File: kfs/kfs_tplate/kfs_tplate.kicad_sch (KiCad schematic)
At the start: 76 parts, among them SW0 SWITCH, SW1 SWITCH, SW10 SWITCH, SW11 SWITCH, SW12 SWITCH, SW13 SWITCH, SW14 SWITCH, SW15 SWITCH, SW16 SWITCH, SW17 SWITCH, SW18 SWITCH, SW19 SWITCH, SW2 SWITCH, SW20 SWITCH, SW21 SWITCH, SW22 SWITCH, SW23 SWITCH, SW24 SWITCH, SW25 SWITCH, SW26 SWITCH, SW27 SWITCH, SW28 SWITCH, SW29 SWITCH, SW3 SWITCH, SW30 SWITCH, SW31 SWITCH, SW32 SWITCH, SW33 SWITCH, SW34 SWITCH, SW35 SWITCH, SW36 SWITCH, SW37 SWITCH, SW38 SWITCH, SW39 SWITCH, SW4 SWITCH, SW40 SWITCH, SW41 SWITCH, SW42 SWITCH, SW43 SWITCH, SW44 SWITCH, SW45 SWITCH, SW46 SWITCH, SW47 SWITCH, SW48 SWITCH, SW49 SWITCH, SW5 SWITCH, SW50 SWITCH, SW51 SWITCH, SW52 SWITCH, SW53 SWITCH, SW54 SWITCH, SW55 SWITCH, SW56 SWITCH, SW57 SWITCH, SW58 SWITCH, SW59 SWITCH, SW6 SWITCH, SW60 SWITCH, SW61 SWITCH, SW62 SWITCH, SW63 SWITCH, SW7 SWITCH, SW8 SWITCH, SW9 SWITCH, U0 ARDUINO_PRO_MICRO

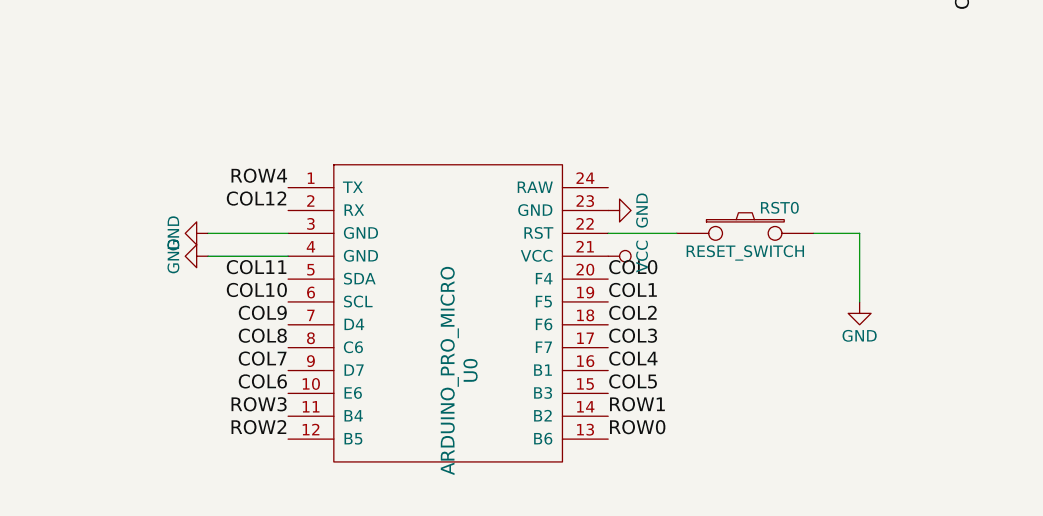
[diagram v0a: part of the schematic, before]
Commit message: Many updates to kfs. Now low profile.
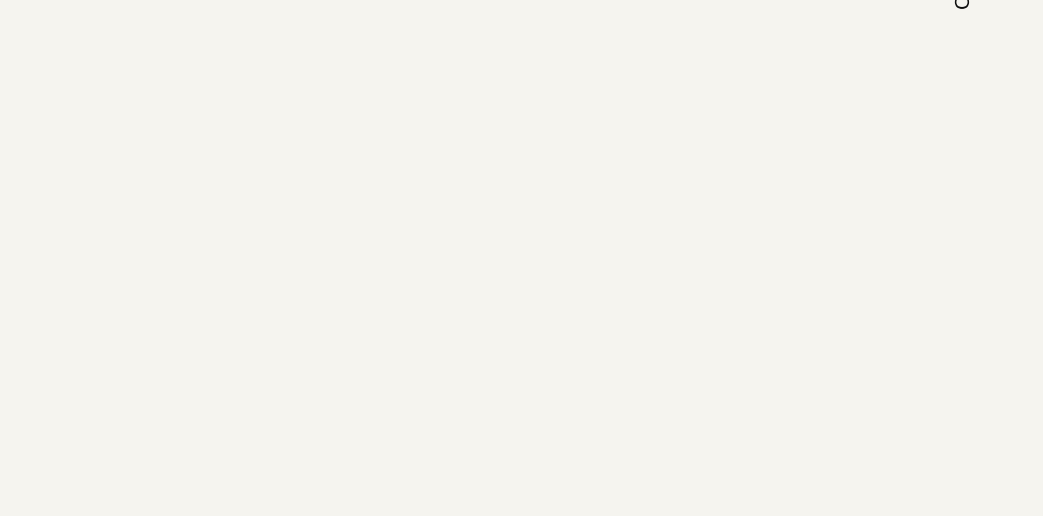
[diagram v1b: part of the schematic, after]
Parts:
- removed RST0: RESET_SWITCH, footprints:reset_button, symbol symbols:SWITCH_PUSH
- removed U0: ARDUINO_PRO_MICRO, ProMicro_v2, symbol symbols:ProMicro
- H0, H10, H2, H3, H4, H5, H6, H7, H8, H9: footprint MountingHole:MountingHole_3.5mm -> MountingHole:MountingHole_2.2mm_M2_ISO7380_Pad
- SW0, SW1, SW10, SW11, SW12, SW13, SW14, SW15, SW16, SW17, SW18, SW19, SW2, SW20, SW21, SW22, SW23, SW24, SW25, SW26, SW27, SW28, SW29, SW3, SW30, SW31, SW32, SW33, SW34, SW35, SW36, SW37, SW38, SW39, SW4, SW40, SW41, SW42, SW43, SW44, SW45, SW46, SW47, SW48, SW49, SW5, SW50, SW51, SW52, SW53, SW54, SW55, SW56, SW57, SW58, SW59, SW6, SW60, SW61, SW62, SW63, SW7, SW8, SW9: footprint footprints:kailh_choc_with_diode -> footprints:kailh_choc_plate

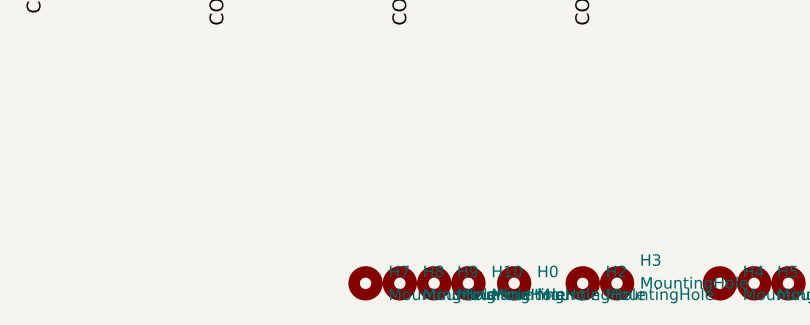
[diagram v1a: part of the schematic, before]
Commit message: Moved the bottom row of kfs farther inward.
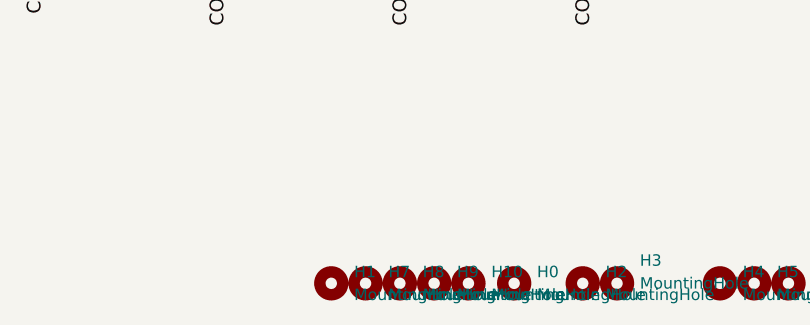
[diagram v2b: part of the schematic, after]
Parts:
- added H1: MountingHole, MountingHole:MountingHole_2.2mm_M2_ISO7380_Pad, symbol Mechanical:MountingHole
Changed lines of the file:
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@@
+    )
+  )
+  (symbol (lib_id "Mechanical:MountingHole") (at 250.19 153.67 0) (unit 1)
+    (in_bom yes) (on_board yes) (dnp no) (fields_autoplaced)
+    (property "Reference" "H1" (at 252.73 152.4 0)
+      (effects (font (size 1.27 1.27)) (justify left))
+    )
+    (property "Value" "MountingHole" (at 252.73 154.94 0)
+      (effects (font (size 1.27 1.27)) (justify left))
+    )
+    (property "Footprint" "MountingHole:MountingHole_2.2mm_M2_ISO7380_Pad" (at 250.19 153.67 0)
+      (effects (font (size 1.27 1.27)) hide)
+    )
+    (property "Datasheet" "~" (at 250.19 153.67 0)
+      (effects (font (size 1.27 1.27)) hide)
+    )
+    (instances
+      (project "kfs_tplate"
+        (path "/97127b28-60f4-45ff-835e-dccfbc833331"
+          (reference "H1") (unit 1)
+        )
+      )
     )
   )

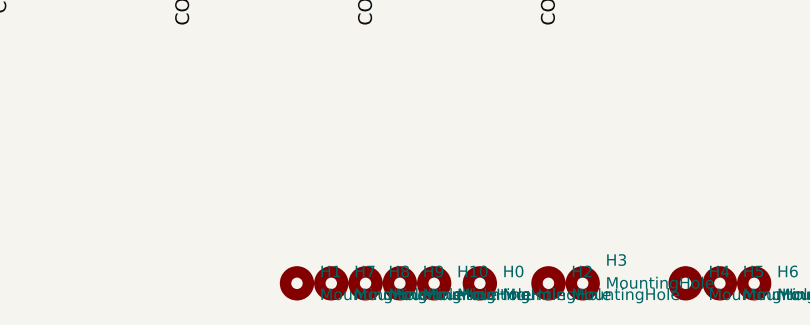
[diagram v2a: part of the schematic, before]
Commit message: Updated reset button and mounting holes on kfs.
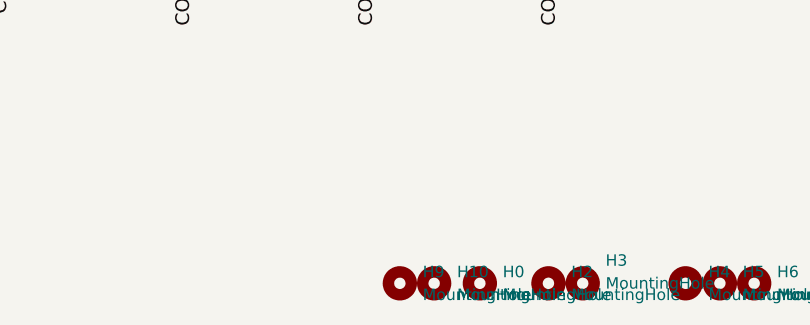
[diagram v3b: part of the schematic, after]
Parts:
- removed H1, H7, H8: MountingHole, MountingHole:MountingHole_2.2mm_M2_ISO7380_Pad, symbol Mechanical:MountingHole
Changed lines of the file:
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@@
-    )
-  )
-  (symbol (lib_id "Mechanical:MountingHole") (at 250.19 153.67 0) (unit 1)
-    (in_bom yes) (on_board yes) (dnp no) (fields_autoplaced)
-    (property "Reference" "H1" (at 252.73 152.4 0)
-      (effects (font (size 1.27 1.27)) (justify left))
-    )
-    (property "Value" "MountingHole" (at 252.73 154.94 0)
-      (effects (font (size 1.27 1.27)) (justify left))
-    )
-    (property "Footprint" "MountingHole:MountingHole_2.2mm_M2_ISO7380_Pad" (at 250.19 153.67 0)
-      (effects (font (size 1.27 1.27)) hide)
-    )
-    (property "Datasheet" "~" (at 250.19 153.67 0)
-      (effects (font (size 1.27 1.27)) hide)
-    )
-    (instances
-      (project "kfs_tplate"
-        (path "/97127b28-60f4-45ff-835e-dccfbc833331"
-          (reference "H1") (unit 1)
-        )
-      )
     )
   )
@@
     )
   )
-  (symbol (lib_id "Mechanical:MountingHole") (at 254 153.67 0) (unit 1)
-    (in_bom yes) (on_board yes) (dnp no) (fields_autoplaced)
-    (property "Reference" "H7" (at 256.54 152.4 0)
-      (effects (font (size 1.27 1.27)) (justify left))
-    )
-    (property "Value" "MountingHole" (at 256.54 154.94 0)
-      (effects (font (size 1.27 1.27)) (justify left))
-    )
-    (property "Footprint" "MountingHole:MountingHole_2.2mm_M2_ISO7380_Pad" (at 254 153.67 0)
-      (effects (font (size 1.27 1.27)) hide)
-    )
-    (property "Datasheet" "~" (at 254 153.67 0)
-      (effects (font (size 1.27 1.27)) hide)
-    )
-    (instances
-      (project "kfs_tplate"
-        (path "/97127b28-60f4-45ff-835e-dccfbc833331"
-          (reference "H7") (unit 1)
-        )
-      )
-    )
-  )
   (symbol (lib_id "symbols:SWITCH_WITH_DIODE") (at 226.06 46.99 0) (unit 1)
     (in_bom yes) (on_board yes) (dnp no) (fields_autoplaced)
@@
         )
       )
-    )
-  )
-  (symbol (lib_id "Mechanical:MountingHole") (at 257.81 153.67 0) (unit 1)
-    (in_bom yes) (on_board yes) (dnp no) (fields_autoplaced)
-    (property "Reference" "H8" (at 260.35 152.4 0)
-      (effects (font (size 1.27 1.27)) (justify left))
-    )
-    (property "Value" "MountingHole" (at 260.35 154.94 0)
-      (effects (font (size 1.27 1.27)) (justify left))
-    )
-    (property "Footprint" "MountingHole:MountingHole_2.2mm_M2_ISO7380_Pad" (at 257.81 153.67 0)
-      (effects (font (size 1.27 1.27)) hide)
-    )
-    (property "Datasheet" "~" (at 257.81 153.67 0)
-      (effects (font (size 1.27 1.27)) hide)
-    )
-    (instances
-      (project "kfs_tplate"
-        (path "/97127b28-60f4-45ff-835e-dccfbc833331"
-          (reference "H8") (unit 1)
-        )
-      )

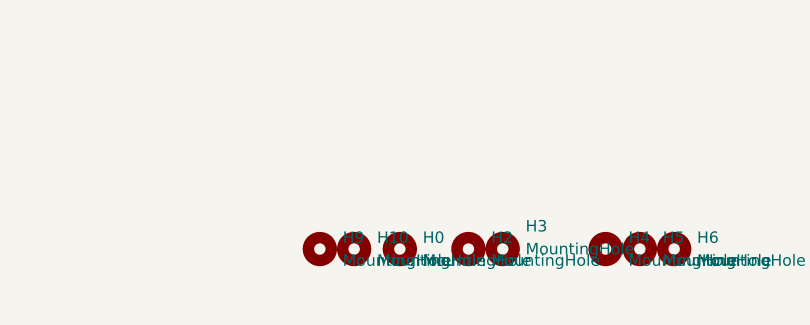
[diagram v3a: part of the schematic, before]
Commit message: Changed reset button again. Removed some standoffs.
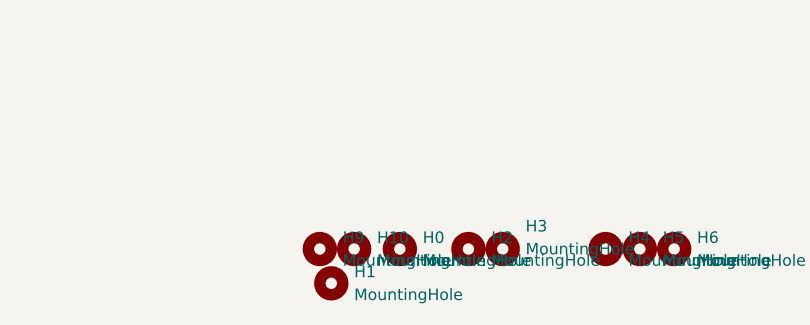
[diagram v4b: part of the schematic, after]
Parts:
- added H1: MountingHole, MountingHole:MountingHole_2.2mm_M2_ISO7380_Pad, symbol Mechanical:MountingHole
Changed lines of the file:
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@@
+    )
+  )
+  (symbol (lib_id "Mechanical:MountingHole") (at 262.89 157.48 0) (unit 1)
+    (in_bom yes) (on_board yes) (dnp no) (fields_autoplaced)
+    (property "Reference" "H1" (at 265.43 156.21 0)
+      (effects (font (size 1.27 1.27)) (justify left))
+    )
+    (property "Value" "MountingHole" (at 265.43 158.75 0)
+      (effects (font (size 1.27 1.27)) (justify left))
+    )
+    (property "Footprint" "MountingHole:MountingHole_2.2mm_M2_ISO7380_Pad" (at 262.89 157.48 0)
+      (effects (font (size 1.27 1.27)) hide)
+    )
+    (property "Datasheet" "~" (at 262.89 157.48 0)
+      (effects (font (size 1.27 1.27)) hide)
+    )
+    (instances
+      (project "kfs_tplate"
+        (path "/97127b28-60f4-45ff-835e-dccfbc833331"
+          (reference "H1") (unit 1)
+        )
+      )
     )
   )

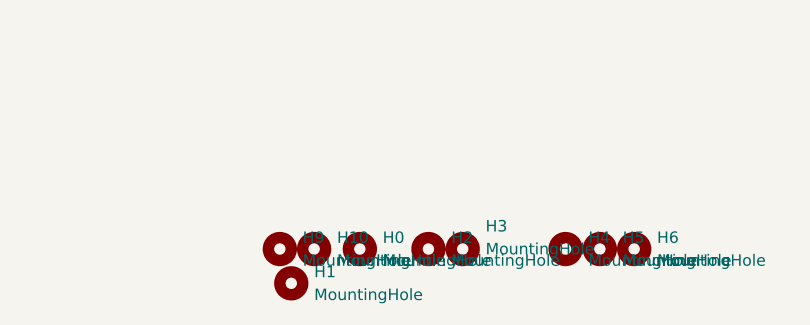
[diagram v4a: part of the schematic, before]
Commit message: Switched kfs to use nice!nano.
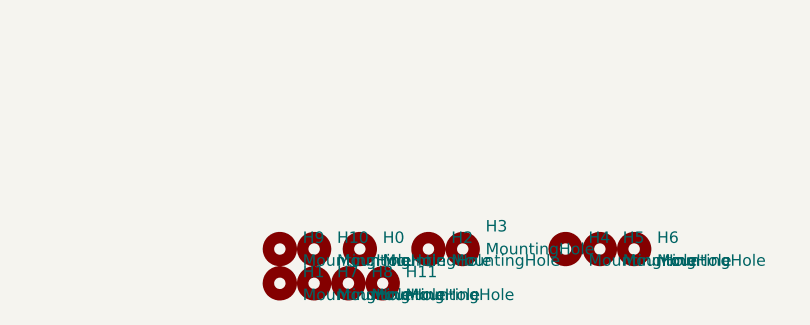
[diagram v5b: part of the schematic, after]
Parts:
- added H11, H7, H8: MountingHole, MountingHole:MountingHole_2.2mm_M2_ISO7380_Pad, symbol Mechanical:MountingHole
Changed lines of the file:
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@@
+    )
+  )
+  (symbol (lib_id "Mechanical:MountingHole") (at 261.62 157.48 0) (unit 1)
+    (in_bom yes) (on_board yes) (dnp no) (fields_autoplaced)
+    (property "Reference" "H1" (at 264.16 156.21 0)
+      (effects (font (size 1.27 1.27)) (justify left))
+    )
+    (property "Value" "MountingHole" (at 264.16 158.75 0)
+      (effects (font (size 1.27 1.27)) (justify left))
+    )
+    (property "Footprint" "MountingHole:MountingHole_2.2mm_M2_ISO7380_Pad" (at 261.62 157.48 0)
+      (effects (font (size 1.27 1.27)) hide)
+    )
+    (property "Datasheet" "~" (at 261.62 157.48 0)
+      (effects (font (size 1.27 1.27)) hide)
+    )
+    (instances
+      (project "kfs_tplate"
+        (path "/97127b28-60f4-45ff-835e-dccfbc833331"
+          (reference "H1") (unit 1)
+        )
+      )
     )
   )
@@
     )
   )
+  (symbol (lib_id "Mechanical:MountingHole") (at 265.43 157.48 0) (unit 1)
+    (in_bom yes) (on_board yes) (dnp no) (fields_autoplaced)
+    (property "Reference" "H7" (at 267.97 156.21 0)
+      (effects (font (size 1.27 1.27)) (justify left))
+    )
+    (property "Value" "MountingHole" (at 267.97 158.75 0)
+      (effects (font (size 1.27 1.27)) (justify left))
+    )
+    (property "Footprint" "MountingHole:MountingHole_2.2mm_M2_ISO7380_Pad" (at 265.43 157.48 0)
+      (effects (font (size 1.27 1.27)) hide)
+    )
+    (property "Datasheet" "~" (at 265.43 157.48 0)
+      (effects (font (size 1.27 1.27)) hide)
+    )
+    (instances
+      (project "kfs_tplate"
+        (path "/97127b28-60f4-45ff-835e-dccfbc833331"
+          (reference "H7") (unit 1)
+        )
+      )
+    )
+  )
   (symbol (lib_id "symbols:SWITCH_WITH_DIODE") (at 144.78 85.09 0) (unit 1)
     (in_bom yes) (on_board yes) (dnp no) (fields_autoplaced)
@@
     )
   )
+  (symbol (lib_id "Mechanical:MountingHole") (at 269.24 157.48 0) (unit 1)
+    (in_bom yes) (on_board yes) (dnp no) (fields_autoplaced)
+    (property "Reference" "H8" (at 271.78 156.21 0)
+      (effects (font (size 1.27 1.27)) (justify left))
+    )
+    (property "Value" "MountingHole" (at 271.78 158.75 0)
+      (effects (font (size 1.27 1.27)) (justify left))
+    )
+    (property "Footprint" "MountingHole:MountingHole_2.2mm_M2_ISO7380_Pad" (at 269.24 157.48 0)
+      (effects (font (size 1.27 1.27)) hide)
+    )
+    (property "Datasheet" "~" (at 269.24 157.48 0)
+      (effects (font (size 1.27 1.27)) hide)
+    )
+    (instances
+      (project "kfs_tplate"
+        (path "/97127b28-60f4-45ff-835e-dccfbc833331"
+          (reference "H8") (unit 1)
+        )
+      )
+    )
+  )
   (symbol (lib_id "symbols:SWITCH_WITH_DIODE") (at 83.82 66.04 0) (unit 1)
     (in_bom yes) (on_board yes) (dnp no) (fields_autoplaced)
@@
     )
   )
-  (symbol (lib_id "Mechanical:MountingHole") (at 262.89 157.48 0) (unit 1)
-    (in_bom yes) (on_board yes) (dnp no) (fields_autoplaced)
-    (property "Reference" "H1" (at 265.43 156.21 0)
-      (effects (font (size 1.27 1.27)) (justify left))
-    )
-    (property "Value" "MountingHole" (at 265.43 158.75 0)
-      (effects (font (size 1.27 1.27)) (justify left))
-    )
-    (property "Footprint" "MountingHole:MountingHole_2.2mm_M2_ISO7380_Pad" (at 262.89 157.48 0)
-      (effects (font (size 1.27 1.27)) hide)
-    )
-    (property "Datasheet" "~" (at 262.89 157.48 0)
-      (effects (font (size 1.27 1.27)) hide)
-    )
-    (instances
-      (project "kfs_tplate"
-        (path "/97127b28-60f4-45ff-835e-dccfbc833331"
-          (reference "H1") (unit 1)
-        )
-      )
-    )
-  )
   (symbol (lib_id "symbols:SWITCH_WITH_DIODE") (at 83.82 85.09 0) (unit 1)
     (in_bom yes) (on_board yes) (dnp no) (fields_autoplaced)
@@
         )
       )
+    )
+  )
+  (symbol (lib_id "Mechanical:MountingHole") (at 273.05 157.48 0) (unit 1)
+    (in_bom yes) (on_board yes) (dnp no) (fields_autoplaced)
+    (property "Reference" "H11" (at 275.59 156.21 0)
+      (effects (font (size 1.27 1.27)) (justify left))
+    )
+    (property "Value" "MountingHole" (at 275.59 158.75 0)
+      (effects (font (size 1.27 1.27)) (justify left))
+    )
+    (property "Footprint" "MountingHole:MountingHole_2.2mm_M2_ISO7380_Pad" (at 273.05 157.48 0)
+      (effects (font (size 1.27 1.27)) hide)
+    )
+    (property "Datasheet" "~" (at 273.05 157.48 0)
+      (effects (font (size 1.27 1.27)) hide)
+    )
+    (instances
+      (project "kfs_tplate"
+        (path "/97127b28-60f4-45ff-835e-dccfbc833331"
+          (reference "H11") (unit 1)
+        )
+      )
